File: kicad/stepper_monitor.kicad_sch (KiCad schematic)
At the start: 54 parts, among them J1 USB_C_Receptacle_USB2.0, J2 Conn_01x02_Male, J3 JTAG, J4 Conn_01x04_Male, J5 Conn_01x04_Male, M1 Motor-simple_stepper_motor_an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, Q1 UMH3N, Q2 PJA3439, SW1 SW_Push, U1 CP2102N-A01-GQFN28, U2 AMS1117-3.3, U3 ESP32-WROOM-32D, U4 5V, U5 CC6920BSO-5A, U6 CC6920BSO-5A

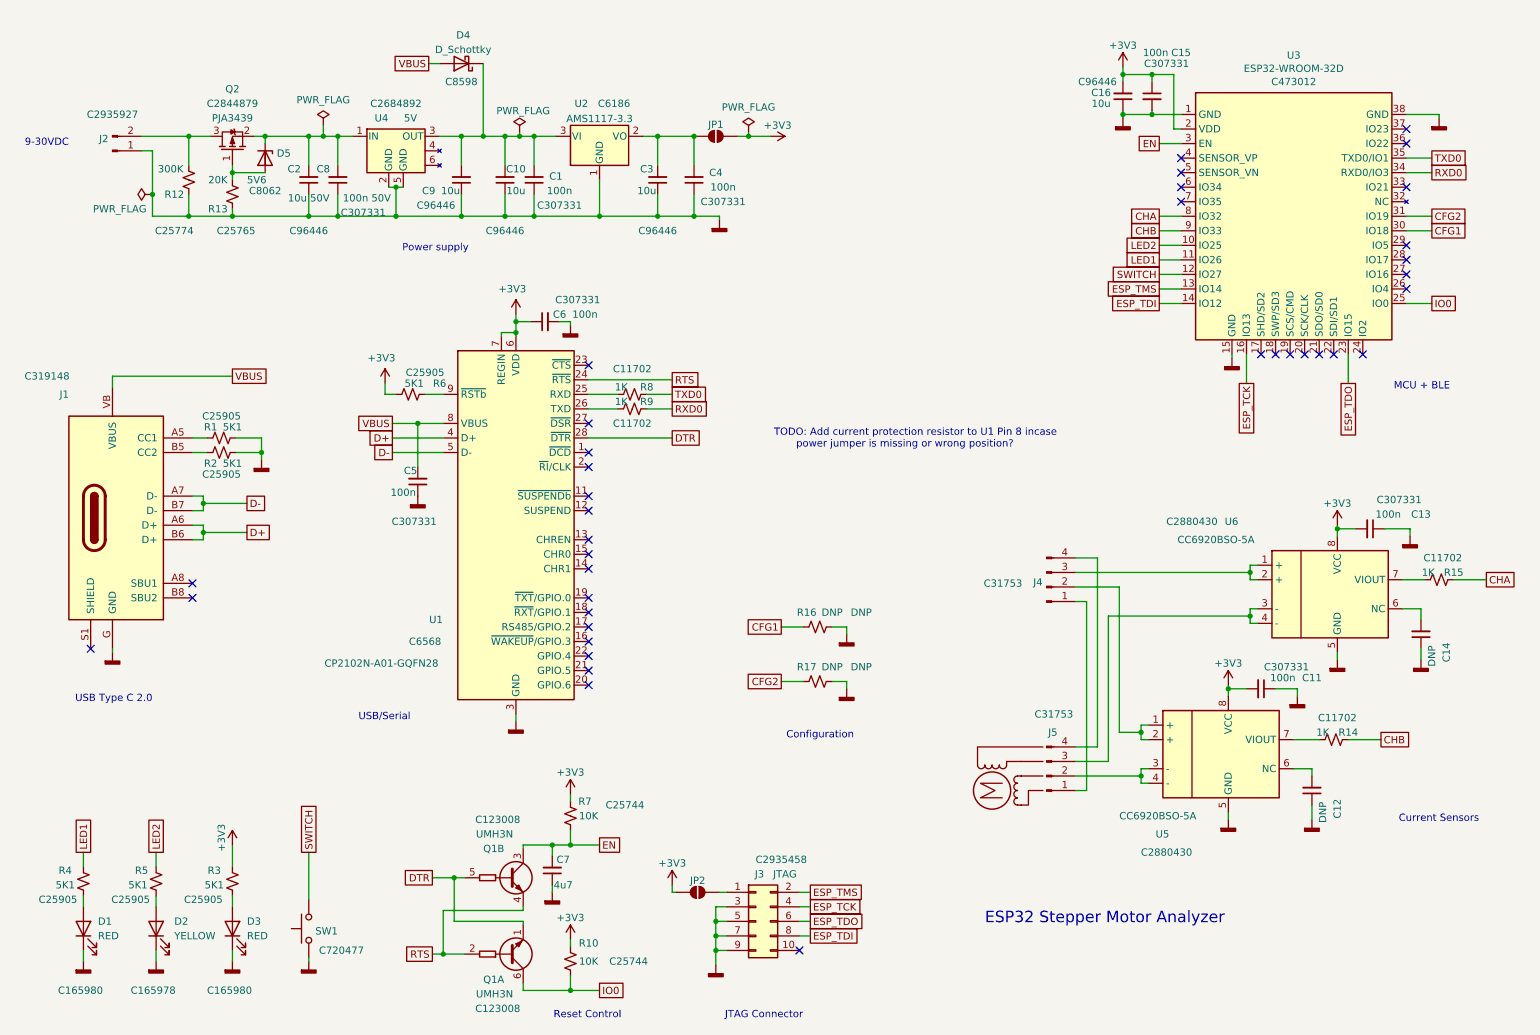
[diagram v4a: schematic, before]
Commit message: Fixed non available JLCPCB parts.
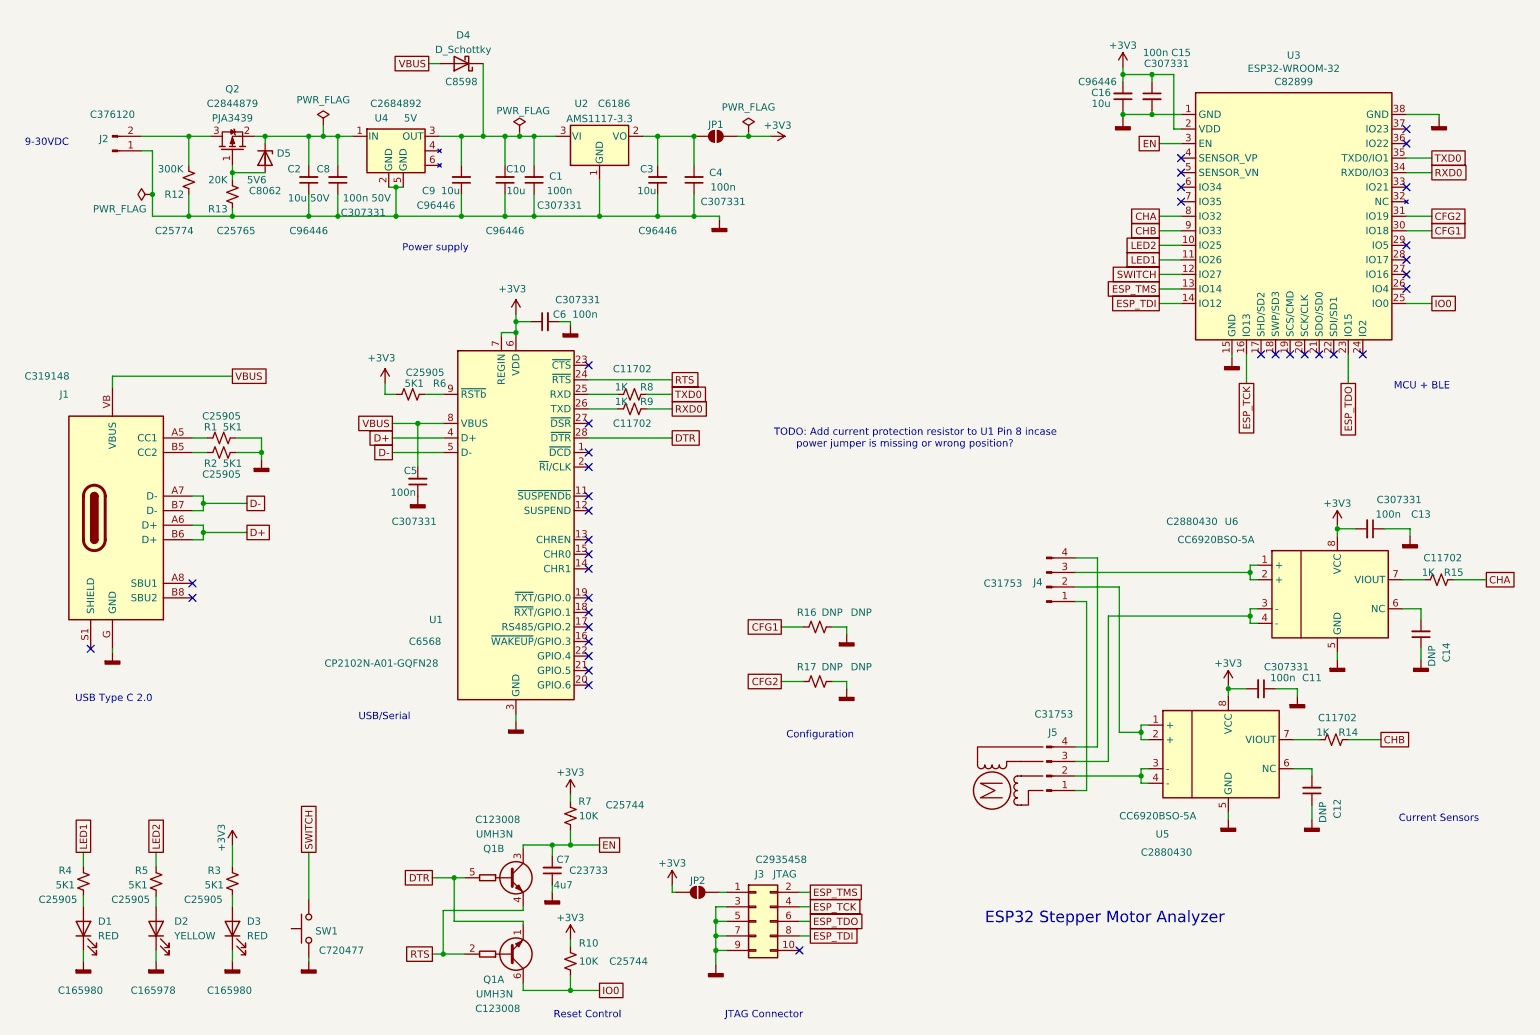
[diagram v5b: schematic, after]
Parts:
- C7: LCSC (none) -> C23733
- J2: LCSC C2935927 -> C376120
- U3: value ESP32-WROOM-32D -> ESP32-WROOM-32; LCSC C473012 -> C82899
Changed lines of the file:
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@@
     (in_bom yes) (on_board yes)
     (property "Reference" "U3" (id 0) (at 239.395 23.3172 0))
-    (property "Value" "ESP32-WROOM-32D" (id 1) (at 239.395 25.6286 0))
+    (property "Value" "ESP32-WROOM-32" (id 1) (at 239.395 25.6286 0))
     (property "Footprint" "stepper_monitor:ESP32-WROOM-32" (id 2) (at 238.76 23.495 0)
       (effects (font (size 1.27 1.27)) hide)
@@
       (effects (font (size 1.27 1.27)) hide)
     )
-    (property "LCSC" "C473012" (id 4) (at 239.395 27.94 0))
+    (property "LCSC" "C82899" (id 4) (at 239.395 27.94 0))
     (pin "1")
     (pin "10")
@@
       (effects (font (size 1.27 1.27)) hide)
     )
-    (property "LCSC" "C2935927" (id 4) (at 33.02 33.655 0))
+    (property "LCSC" "C376120" (id 4) (at 33.02 33.655 0))
     (pin "1")
     (pin "2")
@@
       (effects (font (size 1.27 1.27)) hide)
     )
+    (property "LCSC" "C23733" (id 4) (at 116.205 165.735 0))
     (pin "1")
     (pin "2")
@@
     )
     (path "/00000000-0000-0000-0000-00006319c305"
-      (reference "U3") (unit 1) (value "ESP32-WROOM-32D") (footprint "stepper_monitor:ESP32-WROOM-32")
+      (reference "U3") (unit 1) (value "ESP32-WROOM-32") (footprint "stepper_monitor:ESP32-WROOM-32")
     )
     (path "/c29d3c3c-f637-46cd-b6c9-1a48ecbe9e43"

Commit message: Topologically correct routing. Needs TLC.
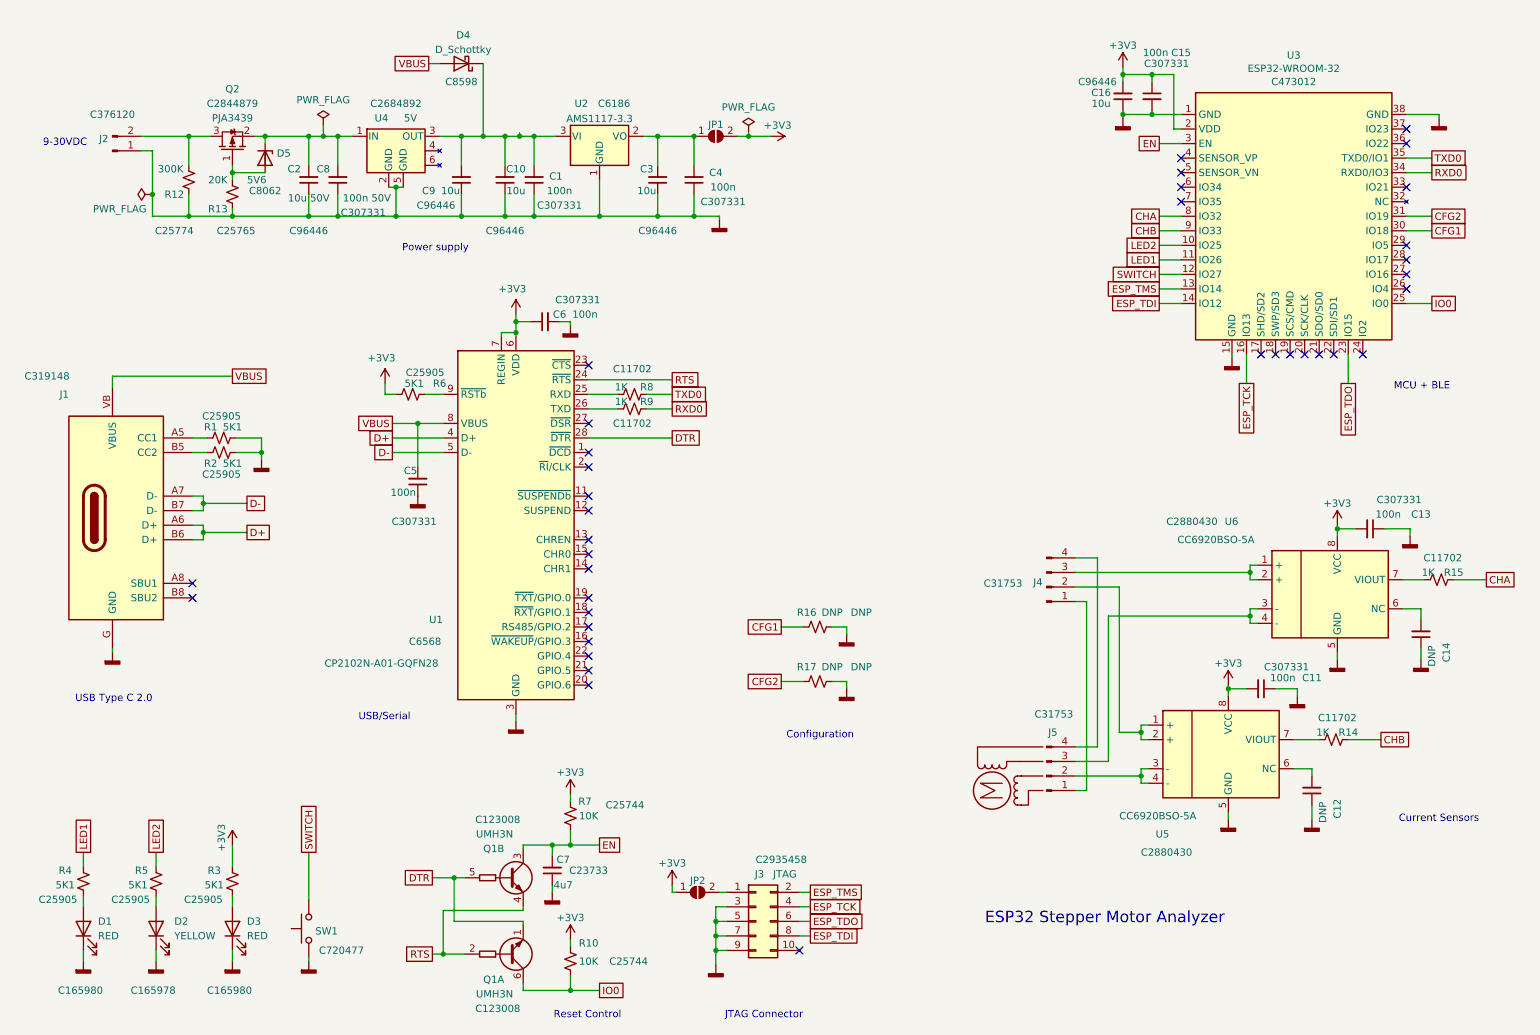
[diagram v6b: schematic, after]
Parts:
- D5: footprint stepper_probe:D_MiniMELF_zenner -> stepper_monitor:D_MiniMELF_zenner
- U1: footprint stepper_monitor:QFN-28-1EP_5x5mm_P0.5mm_EP3.35x3.35mm -> Package_DFN_QFN:QFN-28-1EP_5x5mm_P0.5mm_EP3.35x3.35mm
- U2: footprint Package_TO_SOT_SMD:SOT-223-3_TabPin2 -> stepper_monitor:SOT-223-3_TabPin2
- U3: footprint stepper_monitor:ESP32-WROOM-32 -> RF_Module:ESP32-WROOM-32; LCSC C82899 -> C473012
- U5, U6: footprint stepper_monitor:SOIC-8_3.9x4.9mm_P1.27mm -> Package_SO:SOIC-8_3.9x4.9mm_P1.27mm
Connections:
- no-connect marks 38 -> 37
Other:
- note removed: "TODO: Add current protection resistor to U1 Pin 8 incase power jumper is missing or wrong position?"
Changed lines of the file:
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@@
   (no_connect (at 153.035 179.705))
   (no_connect (at 116.205 113.03))
-  (no_connect (at 29.21 127))
   (no_connect (at 116.205 110.49))
   (no_connect (at 116.205 102.87))
@@
     (effects (font (size 1.27 1.27)) (justify right bottom))
   )
-  (text "TODO: Add current protection resistor to U1 Pin 8 incase \n       power jumper is missing or wrong position?"
-    (at 148.59 92.075 0)
-    (effects (font (size 1.27 1.27)) (justify left bottom))
-  )
   (text "Configuration" (at 162.56 142.875 180)
     (effects (font (size 1.27 1.27)) (justify right bottom))
@@
     (effects (font (size 1.27 1.27)) (justify right bottom))
   )
-  (text "9-30VDC" (at 25.4 39.37 180)
+  (text "9-30VDC" (at 28.575 39.37 180)
     (effects (font (size 1.27 1.27)) (justify right bottom))
   )
@@
     (pin "B8")
     (pin "G")
-    (pin "S1")
     (pin "VB")
   )
@@
     (property "Reference" "U3" (id 0) (at 239.395 23.3172 0))
     (property "Value" "ESP32-WROOM-32" (id 1) (at 239.395 25.6286 0))
-    (property "Footprint" "stepper_monitor:ESP32-WROOM-32" (id 2) (at 238.76 23.495 0)
+    (property "Footprint" "RF_Module:ESP32-WROOM-32" (id 2) (at 238.76 23.495 0)
       (effects (font (size 1.27 1.27)) hide)
     )
@@
       (effects (font (size 1.27 1.27)) hide)
     )
-    (property "LCSC" "C82899" (id 4) (at 239.395 27.94 0))
+    (property "LCSC" "C473012" (id 4) (at 239.395 27.94 0))
     (pin "1")
     (pin "10")
@@
     (property "Reference" "U1" (id 0) (at 89.535 121.92 0))
     (property "Value" "CP2102N-A01-GQFN28" (id 1) (at 80.01 129.54 0))
-    (property "Footprint" "stepper_monitor:QFN-28-1EP_5x5mm_P0.5mm_EP3.35x3.35mm" (id 2) (at 114.935 135.89 0)
+    (property "Footprint" "Package_DFN_QFN:QFN-28-1EP_5x5mm_P0.5mm_EP3.35x3.35mm" (id 2) (at 114.935 135.89 0)
       (effects (font (size 1.27 1.27)) (justify left) hide)
     )
@@
     (pin "2")
   )
-  (symbol (lib_id "power:PWR_FLAG") (at 104.14 36.83 0) (unit 1)
-    (in_bom yes) (on_board yes)
-    (property "Reference" "#FLG01" (id 0) (at 104.14 34.925 0)
-      (effects (font (size 1.27 1.27)) hide)
-    )
-    (property "Value" "PWR_FLAG" (id 1) (at 104.775 33.02 0))
-    (property "Footprint" "" (id 2) (at 104.14 36.83 0)
-      (effects (font (size 1.27 1.27)) hide)
-    )
-    (property "Datasheet" "~" (id 3) (at 104.14 36.83 0)
-      (effects (font (size 1.27 1.27)) hide)
-    )
-    (pin "1")
-  )
   (symbol (lib_id "Regulator_Linear:AMS1117-3.3") (at 118.11 37.465 0) (unit 1)
     (in_bom yes) (on_board yes)
     (property "Reference" "U2" (id 0) (at 114.935 31.75 0))
     (property "Value" "AMS1117-3.3" (id 1) (at 118.11 34.3971 0))
-    (property "Footprint" "Package_TO_SOT_SMD:SOT-223-3_TabPin2" (id 2) (at 118.11 32.385 0)
+    (property "Footprint" "stepper_monitor:SOT-223-3_TabPin2" (id 2) (at 118.11 32.385 0)
       (effects (font (size 1.27 1.27)) hide)
     )
@@
       (effects (font (size 1.27 1.27)) (justify left))
     )
-    (property "Footprint" "stepper_monitor:SOIC-8_3.9x4.9mm_P1.27mm" (id 2) (at 239.395 146.685 0)
+    (property "Footprint" "Package_SO:SOIC-8_3.9x4.9mm_P1.27mm" (id 2) (at 239.395 146.685 0)
       (effects (font (size 1.27 1.27) italic) (justify left) hide)
     )
@@
       (effects (font (size 1.27 1.27)) (justify left))
     )
-    (property "Footprint" "stepper_probe:D_MiniMELF_zenner" (id 2) (at 55.245 41.275 0)
+    (property "Footprint" "stepper_monitor:D_MiniMELF_zenner" (id 2) (at 55.245 41.275 0)
       (effects (font (size 1.27 1.27)) hide)
     )
@@
       (effects (font (size 1.27 1.27)) (justify left))
     )
-    (property "Footprint" "stepper_monitor:SOIC-8_3.9x4.9mm_P1.27mm" (id 2) (at 258.445 118.745 0)
+    (property "Footprint" "Package_SO:SOIC-8_3.9x4.9mm_P1.27mm" (id 2) (at 258.445 118.745 0)
       (effects (font (size 1.27 1.27) italic) (justify left) hide)
     )
@@
     (pin "5")
   )
-  (symbol (lib_id "Jumper:SolderJumper_2_Open") (at 135.255 169.545 0) (unit 1)
+  (symbol (lib_name "SolderJumper_2_Open_1") (lib_id "Jumper:SolderJumper_2_Open") (at 135.255 169.545 0) (unit 1)
     (in_bom no) (on_board yes) (fields_autoplaced)
     (property "Reference" "JP2" (id 0) (at 135.255 167.4932 0))
@@
   )
   (symbol_instances
-    (path "/162e5d8a-3acb-43ed-b5fa-76b65f2a8caa"
-      (reference "#FLG01") (unit 1) (value "PWR_FLAG") (footprint "")
-    )
     (path "/a993f422-2f68-41f7-909b-6e5e01382efd"
       (reference "#FLG0101") (unit 1) (value "PWR_FLAG") (footprint "")
@@
     )
     (path "/c7db2209-f5b4-472f-80a6-506d3059107d"
-      (reference "D5") (unit 1) (value "5V6") (footprint "stepper_probe:D_MiniMELF_zenner")
+      (reference "D5") (unit 1) (value "5V6") (footprint "stepper_monitor:D_MiniMELF_zenner")
     )
     (path "/00000000-0000-0000-0000-00006315a2f3"
@@
     )
     (path "/00000000-0000-0000-0000-0000631b04ca"
-      (reference "U1") (unit 1) (value "CP2102N-A01-GQFN28") (footprint "stepper_monitor:QFN-28-1EP_5x5mm_P0.5mm_EP3.35x3.35mm")
+      (reference "U1") (unit 1) (value "CP2102N-A01-GQFN28") (footprint "Package_DFN_QFN:QFN-28-1EP_5x5mm_P0.5mm_EP3.35x3.35mm")
     )
     (path "/170ecade-8817-49a1-92ea-e91fd90a65e6"
-      (reference "U2") (unit 1) (value "AMS1117-3.3") (footprint "Package_TO_SOT_SMD:SOT-223-3_TabPin2")
+      (reference "U2") (unit 1) (value "AMS1117-3.3") (footprint "stepper_monitor:SOT-223-3_TabPin2")
     )
     (path "/00000000-0000-0000-0000-00006319c305"
-      (reference "U3") (unit 1) (value "ESP32-WROOM-32") (footprint "stepper_monitor:ESP32-WROOM-32")
+      (reference "U3") (unit 1) (value "ESP32-WROOM-32") (footprint "RF_Module:ESP32-WROOM-32")
     )
     (path "/c29d3c3c-f637-46cd-b6c9-1a48ecbe9e43"
@@
     )
     (path "/8e00d3f2-b2b5-4f8f-bf38-86ce986b1bcf"
-      (reference "U5") (unit 1) (value "CC6920BSO-5A") (footprint "stepper_monitor:SOIC-8_3.9x4.9mm_P1.27mm")
+      (reference "U5") (unit 1) (value "CC6920BSO-5A") (footprint "Package_SO:SOIC-8_3.9x4.9mm_P1.27mm")
     )
     (path "/cb5ee068-cc95-4818-84e7-6b246cf90ff1"
-      (reference "U6") (unit 1) (value "CC6920BSO-5A") (footprint "stepper_monitor:SOIC-8_3.9x4.9mm_P1.27mm")
-    )
-  )
+      (reference "U6") (unit 1) (value "CC6920BSO-5A") (footprint "Package_SO:SOIC-8_3.9x4.9mm_P1.27mm")
+    )
+  )

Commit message: Cleaned up the layout.
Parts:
- removed JP2: SolderJumper_2_Open, stepper_monitor:SolderJumper-2_P1.3mm_Open_RoundedPad1.0x1.5mm, symbol Jumper:SolderJumper_2_Open
- D4: footprint Diode_SMD:D_SOD-123 -> stepper_monitor:D_SOD-123
- Q1: footprint Package_TO_SOT_SMD:SOT-363_SC-70-6 -> stepper_monitor:SOT-363_SC-70-6
- U1: footprint Package_DFN_QFN:QFN-28-1EP_5x5mm_P0.5mm_EP3.35x3.35mm -> stepper_monitor:QFN-28-1EP_5x5mm_P0.5mm_EP3.35x3.35mm
- U3: footprint RF_Module:ESP32-WROOM-32 -> stepper_monitor:ESP32-WROOM-32; LCSC C473012 -> C82899
- U5, U6: footprint Package_SO:SOIC-8_3.9x4.9mm_P1.27mm -> stepper_monitor:SOIC-8_3.9x4.9mm_P1.27mm
- renumbered J4 to J1, J5 to J2, J2 to J3, J1 to J4, J3 to J5
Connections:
- no-connect marks 37 -> 38

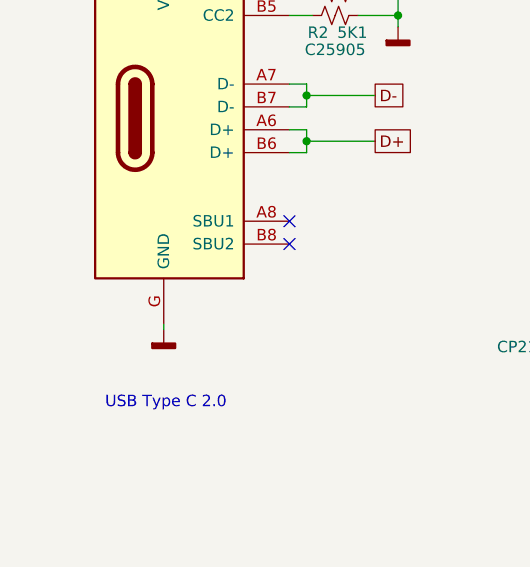
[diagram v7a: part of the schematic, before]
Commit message: Connected USB shield to ground.
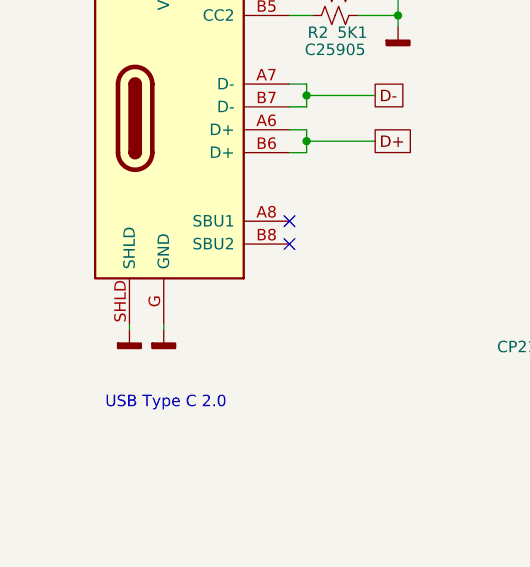
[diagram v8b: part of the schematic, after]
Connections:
- net GNDD: now also J4.SHLD
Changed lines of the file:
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@@
+    (stroke (width 0) (type default) (color 0 0 0 0))
+  )
+  (wire (pts (xy 29.21 127) (xy 29.21 127.635))
     (stroke (width 0) (type default) (color 0 0 0 0))
   )
@@
     (pin "B8")
     (pin "G")
+    (pin "SHLD")
     (pin "VB")
   )
@@
     (pin "4")
   )
+  (symbol (lib_id "power:GNDD") (at 29.21 127.635 0) (unit 1)
+    (in_bom yes) (on_board yes)
+    (property "Reference" "#PWR0101" (id 0) (at 29.21 133.985 0)
+      (effects (font (size 1.27 1.27)) hide)
+    )
+    (property "Value" "GNDD" (id 1) (at 29.3116 131.572 0)
+      (effects (font (size 1.27 1.27)) hide)
+    )
+    (property "Footprint" "" (id 2) (at 29.21 127.635 0)
+      (effects (font (size 1.27 1.27)) hide)
+    )
+    (property "Datasheet" "" (id 3) (at 29.21 127.635 0)
+      (effects (font (size 1.27 1.27)) hide)
+    )
+    (pin "1")
+  )
   (symbol (lib_id "stepper_monitor:Motor-simple_stepper_motor_analyzer") (at 189.23 151.765 90) (unit 1)
     (in_bom no) (on_board no) (fields_autoplaced)
@@
       (reference "#PWR017") (unit 1) (value "GNDD") (footprint "")
     )
+    (path "/5d3263f0-2044-4033-8250-d44c87ba32dc"
+      (reference "#PWR0101") (unit 1) (value "GNDD") (footprint "")
+    )
     (path "/00000000-0000-0000-0000-000063145fda"
